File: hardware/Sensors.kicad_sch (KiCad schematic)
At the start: 16 parts, among them IC201 APDS-9306-065, IC202 BMI270, IC203 BMP581, IC204 LIS2MDLTR, Q201 DMG1013UW-7

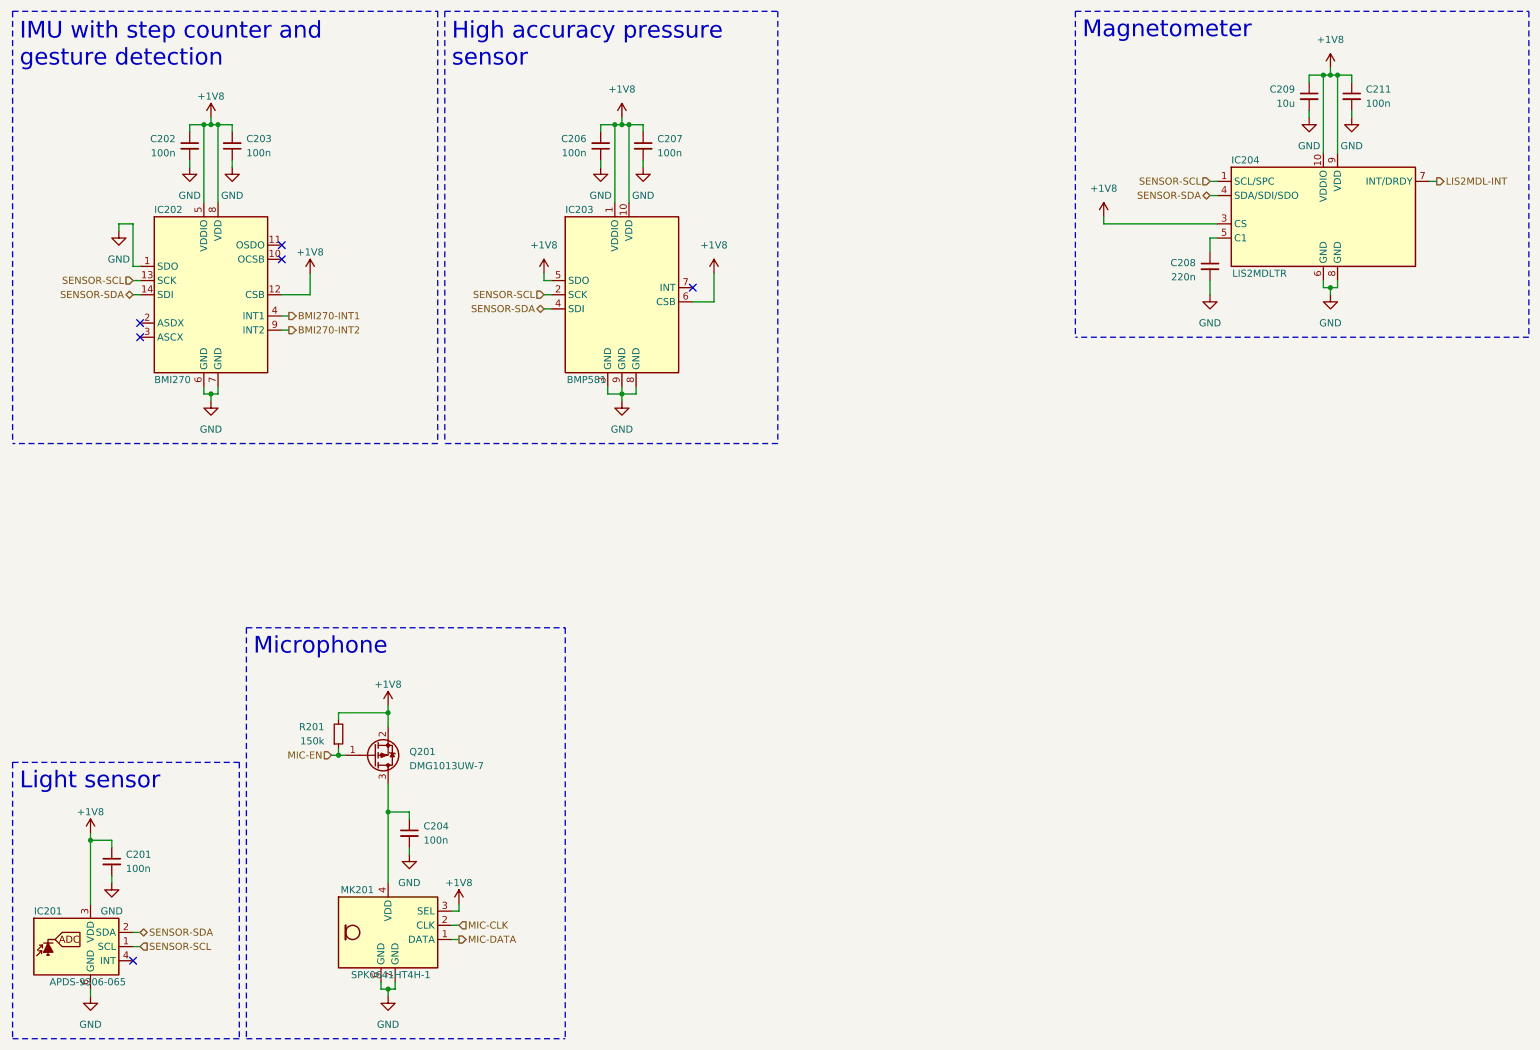
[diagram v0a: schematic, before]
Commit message: KiBot: Enhance KiBot configuration
- Implement #110
- Implement #109
- Add refresh for PCB specifications
- Add refresh for stackup

Signed-off-by: Daniel Kampert <danielkampert@kampis-elektroecke.de>
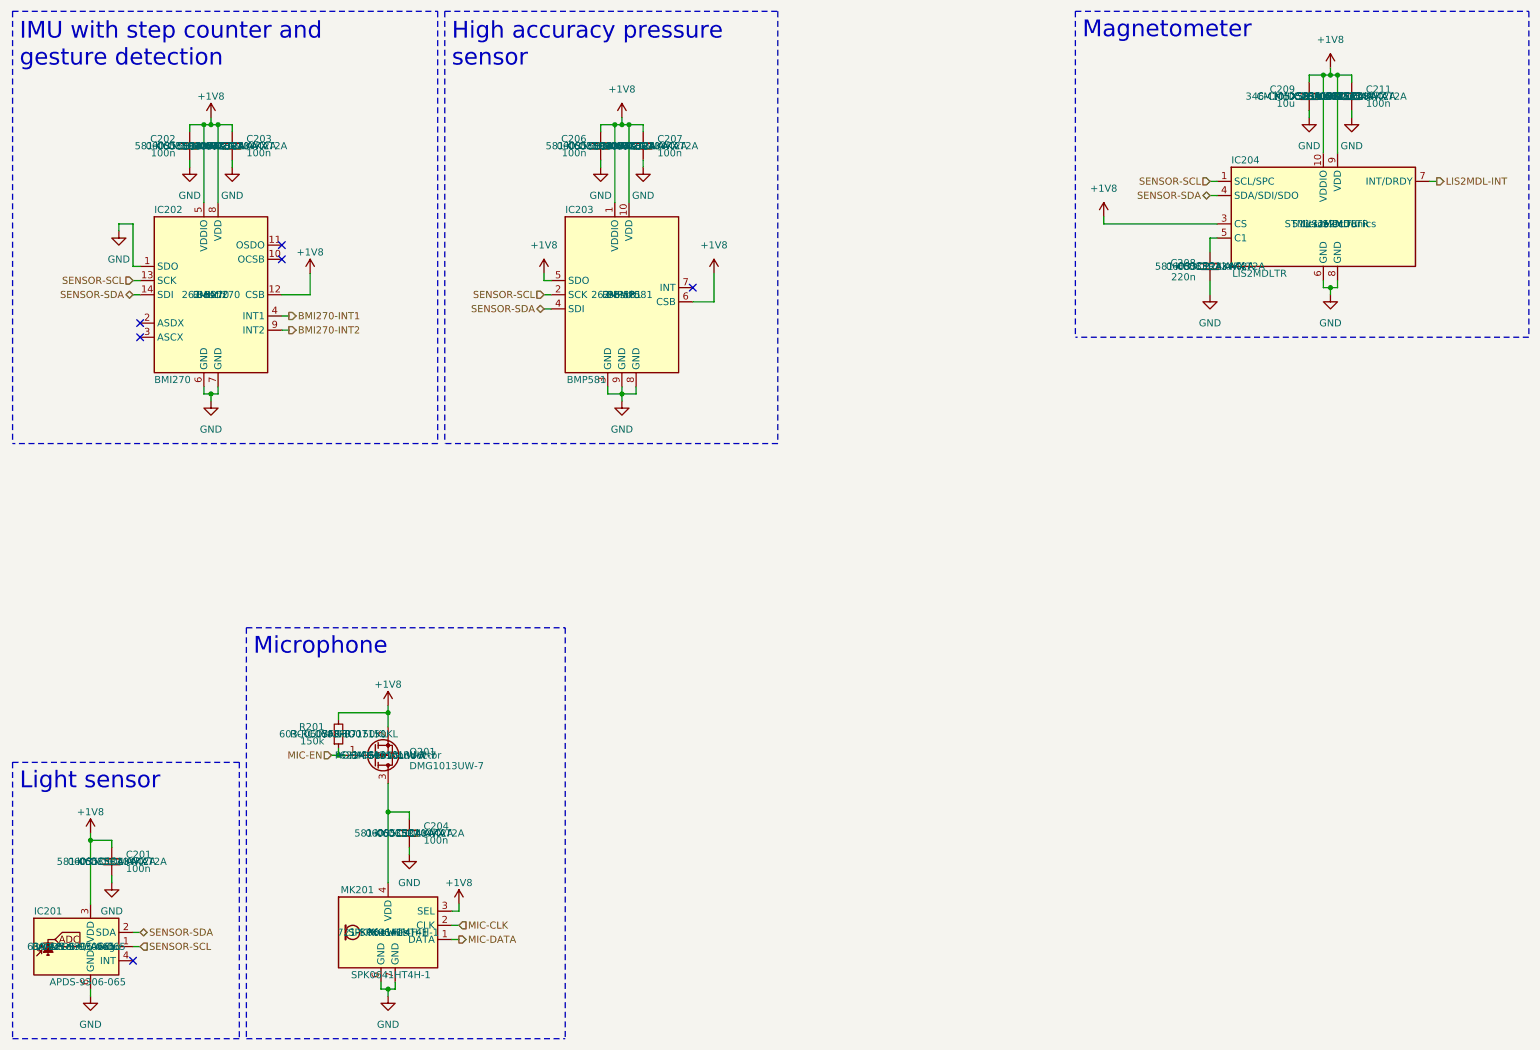
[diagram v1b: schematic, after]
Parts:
- C201, C202, C203, C204, C206, C207, C211: Mfr. KYOCERA AVX -> (none); Mfr. No. 06035C104KAT2A -> (none); Order Number 581-06035C104KAT2A -> (none); manf (none) -> KYOCERA AVX; manf# (none) -> 06035C104KAT2A; mouser# (none) -> 581-06035C104KAT2A
- C208: Mfr. KYOCERA AVX -> (none); Mfr. No. 06033C224KAT2A -> (none); Order Number 581-06033C224KAT2A -> (none); manf (none) -> KYOCERA AVX; manf# (none) -> 06033C224KAT2A; mouser# (none) -> 581-06033C224KAT2A
- C209: Mfr. KYOCERA AVX -> (none); Mfr. No. CM105X5R106M25AT -> (none); Order Number 346-CM105X5R106M25AT -> (none); manf (none) -> KYOCERA AVX; manf# (none) -> CM105X5R106M25AT; mouser# (none) -> 346-CM105X5R106M25AT
- IC201: Mfr. Broadcom / Avago -> (none); Mfr. No. APDS-9306-065 -> (none); Order Number 630-APDS-9306-065 -> (none); manf (none) -> Broadcom / Avago; manf# (none) -> APDS-9306-065; mouser# (none) -> 630-APDS-9306-065
- IC202: Mfr. Bosch -> (none); Mfr. No. BMI270 -> (none); Order Number 262-BMI270 -> (none); manf (none) -> Bosch; manf# (none) -> BMI270; mouser# (none) -> 262-BMI270
- IC203: Mfr. Bosch -> (none); Mfr. No. BMP581 -> (none); Order Number 262-BMP581 -> (none); manf (none) -> Bosch; manf# (none) -> BMP581; mouser# (none) -> 262-BMP581
- IC204: Mfr. STMicroelectronics -> (none); Mfr. No. LIS2MDLTR -> (none); Order Number 511-LIS2MDLTR -> (none); manf (none) -> STMicroelectronics; manf# (none) -> LIS2MDLTR; mouser# (none) -> 511-LIS2MDLTR
- MK201: Mfr. Knowles -> (none); Mfr. No. SPK0641HT4H-1 -> (none); Order Number 721-SPK0641HT4H-1 -> (none); manf (none) -> Knowles; manf# (none) -> SPK0641HT4H-1; mouser# (none) -> 721-SPK0641HT4H-1
- Q201: Mfr. ROHM Semiconductor -> (none); Mfr. No. DMG1013UW-7 -> (none); Order Number 621-DMG1013UW-7 -> (none); manf (none) -> ROHM Semiconductor; manf# (none) -> DMG1013UW-7; mouser# (none) -> 621-DMG1013UW-7
- R201: Mfr. YAGEO -> (none); Mfr. No. RC0603FR-07150KL -> (none); Order Number 603-RC0603FR-07150KL -> (none); manf (none) -> YAGEO; manf# (none) -> RC0603FR-07150KL; mouser# (none) -> 603-RC0603FR-07150KL
